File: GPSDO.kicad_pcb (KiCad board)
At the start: 2 copper layers, 85 x 85 mm, 100 parts, among them J1 Conn_Coaxial, J10 Conn_Coaxial, J2 Barrel_Jack, J3 PROG, J4 DISP_MODULE, J5 GPS_CONN, J6 Conn_Coaxial, J7 Conn_Coaxial, J8 Conn_Coaxial, J9 Conn_Coaxial, SW1 RESET_BTN, U1 REF3450, U10 AVR32DB28x-xSO, U11 AZ1117H-5.0TRG1, U12 AZ1117H-5.0TRG1, U13 74HC390, U14 DS34C87T, U15 MCP6486T-E/OT, U2 74AUC2G04, U3 74AUC2G04, U4 74AUC1G74, U5 AD5680, U6 NB3N551MN, U7 74LVC1G125SE-7, U8 74LVC1G125SE-7, U9 LTC2050IS8, X1 OC5SC25

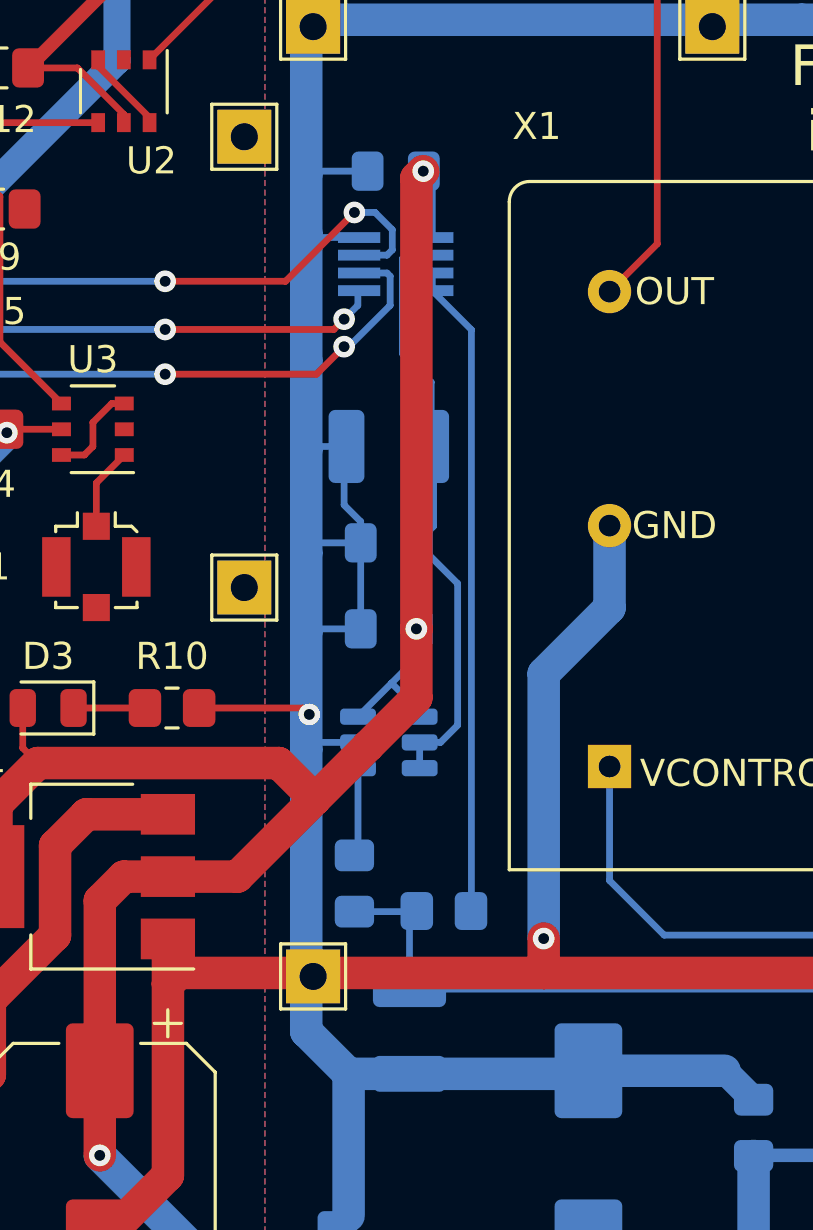
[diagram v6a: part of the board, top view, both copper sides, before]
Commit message: TODO: ref/ADC/opamp placement
The layout for those components is far from optimal
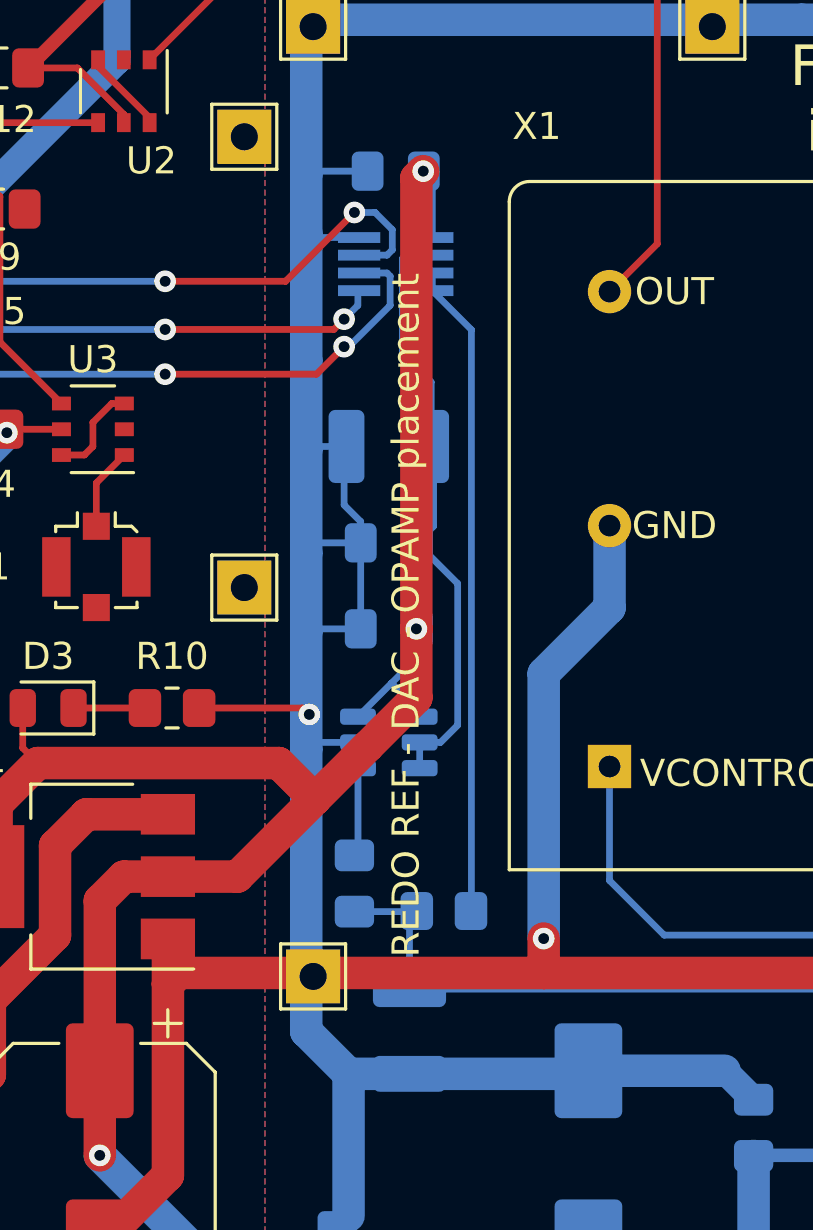
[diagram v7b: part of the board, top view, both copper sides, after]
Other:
- board text added: "REDO REF - DAC - OPAMP placement"
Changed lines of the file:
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@@
+    (effects (font (size 1 1) (thickness 0.15)))
+  )
+  (gr_text "REDO REF - DAC - OPAMP placement" (at 69.723 79.121 90) (layer "F.SilkS")
     (effects (font (size 1 1) (thickness 0.15)))
   )

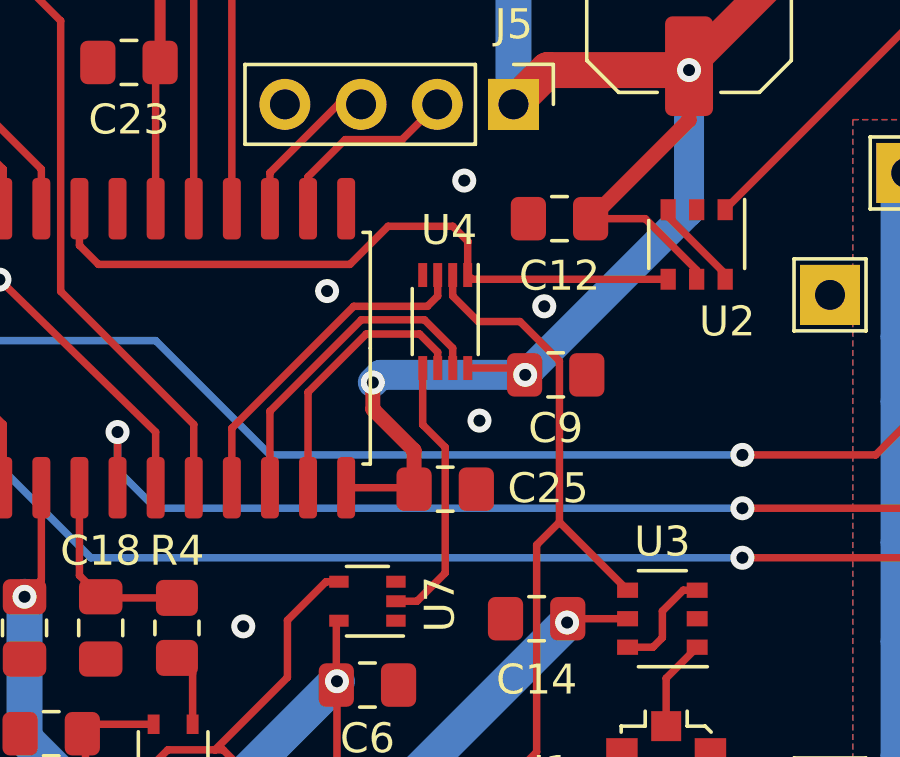
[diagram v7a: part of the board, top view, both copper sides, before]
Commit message: Flip-flop error
Wrong device, wasn't 5V tolerant. Corrected
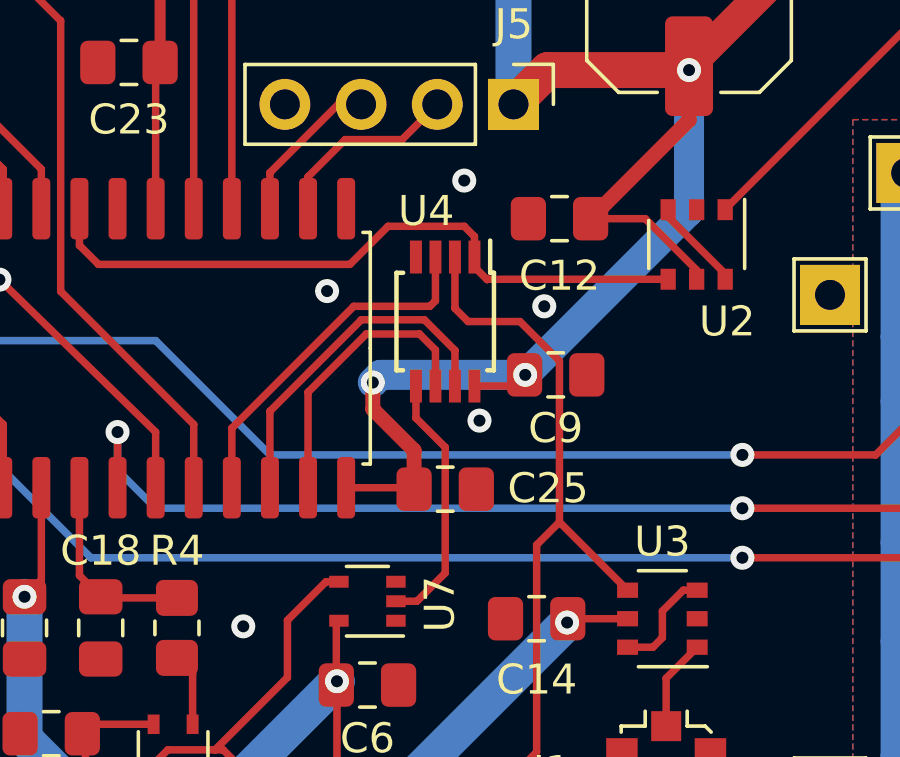
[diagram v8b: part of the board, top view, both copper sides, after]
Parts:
- U1: value REF3450 -> REF3440IDBVR
- U4: value 74AUC1G74 -> 74LVC2G74DP,125; footprint Package_SO:VSSOP-8_2.3x2mm_P0.5mm -> Package_SO:TSSOP-8_3x3mm_P0.65mm
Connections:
- H1 pad 1: GND -> (no net)
- H2 pad 1: GND -> (no net)
- H3 pad 1: GND -> (no net)
- U7 pad 4: Net-(R3-Pad1) -> Net-(U7-Pad4)
- U8 pad 1: Net-(R3-Pad1) -> Net-(U7-Pad4)
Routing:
- net Net-(U7-Pad4): track 0.00 -> 12.5 mm
- net Net-(R3-Pad1): track 12.5 -> 0.00 mm
- net /PPS_SIG: track 36.6 -> 37.4 mm
- net /FF_SET: track 11.0 -> 11.6 mm
- net /ICP1: track 11.4 -> 12.0 mm
- net /FF_RESET: track 9.09 -> 9.66 mm
- net Net-(U4-Pad5): track 9.17 -> 8.67 mm
